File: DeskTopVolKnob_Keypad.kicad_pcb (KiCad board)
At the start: 2 copper layers, 118.4 x 101.6 mm, 105 parts, among them J1 DX07S016JA1R1500, SW1 Rotary_Encoder_Switch, SW10 SW, SW11 SW, SW12 SW, SW13 SW, SW14 SW, SW15 SW, SW16 SW, SW17 SW, SW18 SW, SW19 SW, SW2 SW, SW20 SW, SW21 SW, SW22 SW, SW23 SW, SW24 SW, SW25 SW, SW26 SW, SW27 SW_Push, SW3 SW, SW4 SW, SW5 SW, SW6 SW, SW7 SW, SW8 SW, SW9 SW, U1 ATmega32U4-AU, Y1 16MHz

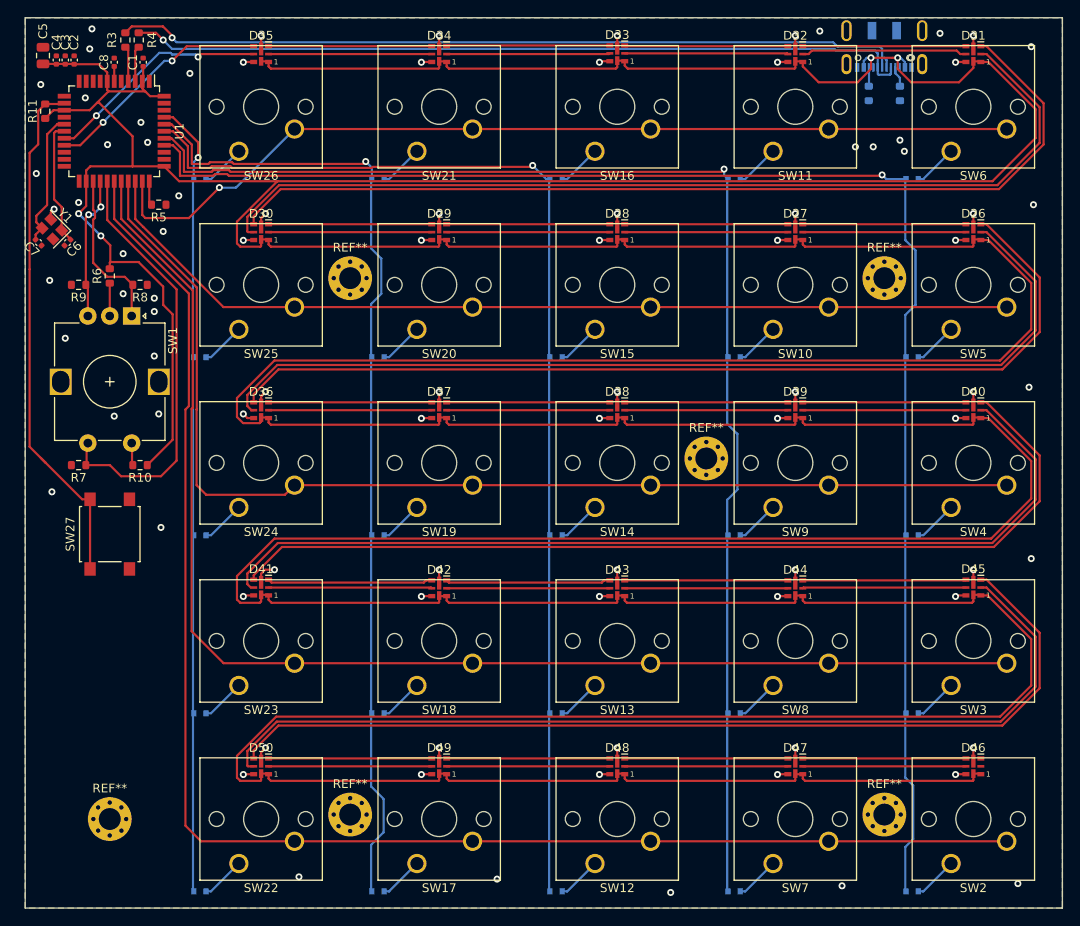
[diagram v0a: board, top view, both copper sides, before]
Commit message: new LEDs and crystal cap fixed
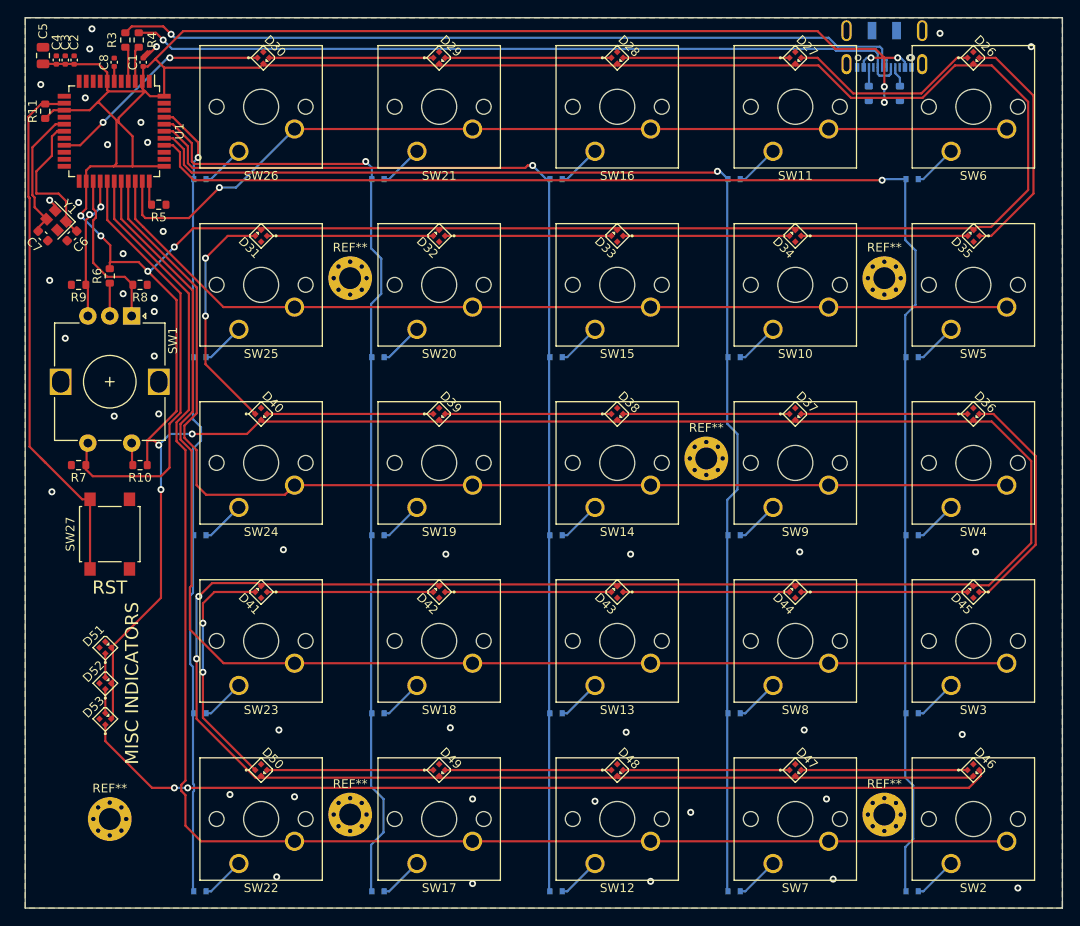
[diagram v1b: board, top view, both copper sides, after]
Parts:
- added D51: SK6805-EC-15, Special Partd:SK6805-EC-15, F.Cu at (45.7, 99.8)
- added D52: SK6805-EC-15, Special Partd:SK6805-EC-15, F.Cu at (45.7, 103.9)
- added D53: SK6805-EC-15, Special Partd:SK6805-EC-15, F.Cu at (45.7, 108.0)
- C6, C7: footprint Capacitor_SMD:C_0402_1005Metric -> Capacitor_SMD:C_0603_1608Metric
- D26, D27, D28, D29, D30, D31, D32, D33, D34, D35, D36, D37, D38, D39, D40, D41, D42, D43, D44, D45, D46, D47, D48, D49, D50: value APA102-2020 -> SK6805-EC-15; footprint LED_SMD:LED-APA102-2020 -> Special Partd:SK6805-EC-15
- SW10, SW11, SW12, SW13, SW14, SW15, SW16, SW17, SW18, SW19, SW2, SW20, SW21, SW22, SW23, SW24, SW25, SW26, SW3, SW4, SW5, SW6, SW7, SW8, SW9: footprint Downloaded parts:SW_Cherry_MX_1.00u_PCB -> Button_Switch_Keyboard:SW_Cherry_MX_1.00u_PCB
- moved D35 83.9 mm to (144.8, 52.8), turned to 135 degrees
- moved D31 83.9 mm to (63.5, 52.8), turned to 135 degrees
- moved D36 81.3 mm to (144.8, 73.2), turned to 315 degrees
- moved D40 81.3 mm to (63.5, 73.2), turned to 315 degrees
- moved D32 45.6 mm to (83.8, 52.8), turned to 135 degrees
- moved D34 45.6 mm to (124.5, 52.8), turned to 135 degrees
- moved D37 40.6 mm to (124.5, 73.2), turned to 315 degrees
- moved D39 40.6 mm to (83.8, 73.2), turned to 315 degrees
- moved D33 20.8 mm to (104.1, 52.8), turned to 135 degrees
- moved D30 19.9 mm to (63.8, 32.5), turned to 315 degrees
- moved D26 19.9 mm to (144.8, 32.5), turned to 315 degrees
- moved D27 19.9 mm to (124.5, 32.5), turned to 315 degrees
- moved D28 19.9 mm to (104.1, 32.5), turned to 315 degrees
- moved D29 19.9 mm to (83.8, 32.5), turned to 315 degrees
- moved Y1 1.14 mm to (40.1, 51.1)
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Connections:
- D26 pad 1: +5V -> Net-(D26-Pad1)
- D26 pad 2: Net-(D26-Pad2) -> +5V
- D26 pad 4: Net-(D26-Pad4) -> GND
- D27 pad 1: +5V -> Net-(D27-Pad1)
- D27 pad 2: Net-(D26-Pad5) -> +5V
- D27 pad 3: Net-(D26-Pad4) -> Net-(D26-Pad1)
- D27 pad 4: Net-(D27-Pad4) -> GND
- D28 pad 1: +5V -> Net-(D28-Pad1)
- D28 pad 2: Net-(D27-Pad5) -> +5V
- D28 pad 3: Net-(D27-Pad4) -> Net-(D27-Pad1)
- D28 pad 4: Net-(D28-Pad4) -> GND
- D29 pad 1: +5V -> Net-(D29-Pad1)
- D29 pad 2: Net-(D28-Pad5) -> +5V
- D29 pad 3: Net-(D28-Pad4) -> Net-(D28-Pad1)
- D29 pad 4: Net-(D29-Pad4) -> GND
- D30 pad 1: +5V -> /LEDs/SD
- D30 pad 2: Net-(D29-Pad5) -> +5V
- D30 pad 3: Net-(D29-Pad4) -> Net-(D29-Pad1)
- D30 pad 4: Net-(D30-Pad4) -> GND
- D31 pad 1: +5V -> Net-(D31-Pad1)
- D31 pad 2: Net-(D30-Pad5) -> +5V
- D31 pad 3: Net-(D30-Pad4) -> Net-(D31-Pad3)
- D31 pad 4: Net-(D31-Pad4) -> GND
- D32 pad 1: +5V -> Net-(D32-Pad1)
- D32 pad 2: Net-(D31-Pad5) -> +5V
- D32 pad 3: Net-(D31-Pad4) -> Net-(D31-Pad1)
- D32 pad 4: Net-(D32-Pad4) -> GND
- D33 pad 1: +5V -> Net-(D33-Pad1)
- D33 pad 2: Net-(D32-Pad5) -> +5V
- D33 pad 3: Net-(D32-Pad4) -> Net-(D32-Pad1)
- D33 pad 4: Net-(D33-Pad4) -> GND
- D34 pad 1: +5V -> Net-(D34-Pad1)
- D34 pad 2: Net-(D33-Pad5) -> +5V
- D34 pad 3: Net-(D33-Pad4) -> Net-(D33-Pad1)
- D34 pad 4: Net-(D34-Pad4) -> GND
- D35 pad 1: +5V -> Net-(D26-Pad3)
- D35 pad 2: Net-(D34-Pad5) -> +5V
- D35 pad 3: Net-(D34-Pad4) -> Net-(D34-Pad1)
- D35 pad 4: /LEDs/SD -> GND
- D36 pad 1: +5V -> Net-(D36-Pad1)
- D36 pad 2: Net-(D36-Pad2) -> +5V
- D36 pad 4: Net-(D26-Pad3) -> GND
- D37 pad 1: +5V -> Net-(D37-Pad1)
- D37 pad 2: Net-(D37-Pad2) -> +5V
- D37 pad 3: Net-(D37-Pad3) -> Net-(D36-Pad1)
- D37 pad 4: Net-(D36-Pad3) -> GND
- D38 pad 1: +5V -> Net-(D38-Pad1)
- D38 pad 2: Net-(D38-Pad2) -> +5V
- D38 pad 3: Net-(D38-Pad3) -> Net-(D37-Pad1)
- D38 pad 4: Net-(D37-Pad3) -> GND
- D39 pad 1: +5V -> Net-(D39-Pad1)
- D39 pad 2: Net-(D39-Pad2) -> +5V
- D39 pad 3: Net-(D39-Pad3) -> Net-(D38-Pad1)
- D39 pad 4: Net-(D38-Pad3) -> GND
- D40 pad 1: +5V -> Net-(D31-Pad3)
- D40 pad 2: Net-(D40-Pad2) -> +5V
- D40 pad 3: Net-(D40-Pad3) -> Net-(D39-Pad1)
- D40 pad 4: Net-(D39-Pad3) -> GND
- D41 pad 1: +5V -> Net-(D41-Pad1)
- D41 pad 2: Net-(D41-Pad2) -> +5V
- D41 pad 4: Net-(D40-Pad3) -> GND
- D42 pad 1: +5V -> Net-(D42-Pad1)
- D42 pad 2: Net-(D42-Pad2) -> +5V
- D42 pad 3: Net-(D42-Pad3) -> Net-(D41-Pad1)
- D42 pad 4: Net-(D41-Pad3) -> GND
- D43 pad 1: +5V -> Net-(D43-Pad1)
- D43 pad 2: Net-(D43-Pad2) -> +5V
- D43 pad 3: Net-(D43-Pad3) -> Net-(D42-Pad1)
- D43 pad 4: Net-(D42-Pad3) -> GND
- D44 pad 1: +5V -> Net-(D44-Pad1)
- D44 pad 2: Net-(D44-Pad2) -> +5V
- D44 pad 3: Net-(D44-Pad3) -> Net-(D43-Pad1)
- D44 pad 4: Net-(D43-Pad3) -> GND
- D45 pad 1: +5V -> Net-(D36-Pad3)
- D45 pad 2: Net-(D45-Pad2) -> +5V
- D45 pad 3: Net-(D45-Pad3) -> Net-(D44-Pad1)
- D45 pad 4: Net-(D44-Pad3) -> GND
- D46 pad 1: +5V -> Net-(D46-Pad1)
- D46 pad 2: (no net) -> +5V
- D46 pad 3: (no net) -> Net-(D46-Pad3)
- D46 pad 4: Net-(D46-Pad4) -> GND
- D47 pad 1: +5V -> Net-(D47-Pad1)
- D47 pad 2: Net-(D46-Pad5) -> +5V
- D47 pad 3: Net-(D46-Pad4) -> Net-(D46-Pad1)
- D47 pad 4: Net-(D47-Pad4) -> GND
- D48 pad 1: +5V -> Net-(D48-Pad1)
- D48 pad 2: Net-(D47-Pad5) -> +5V
- D48 pad 3: Net-(D47-Pad4) -> Net-(D47-Pad1)
- D48 pad 4: Net-(D48-Pad4) -> GND
- D49 pad 1: +5V -> Net-(D49-Pad1)
- D49 pad 2: Net-(D48-Pad5) -> +5V
- D49 pad 3: Net-(D48-Pad4) -> Net-(D48-Pad1)
- D49 pad 4: Net-(D49-Pad4) -> GND
- D50 pad 1: +5V -> Net-(D41-Pad3)
- D50 pad 2: Net-(D49-Pad5) -> +5V
- D50 pad 3: Net-(D49-Pad4) -> Net-(D49-Pad1)
- D50 pad 4: Net-(D45-Pad3) -> GND
- J1 pad 10: (no net) -> Net-(J1-Pad10)
- J1 pad 4: (no net) -> Net-(J1-Pad4)
- U1 pad 1: (no net) -> Net-(U1-Pad1)
- U1 pad 10: (no net) -> Net-(U1-Pad10)
- U1 pad 11: (no net) -> Net-(U1-Pad11)
- U1 pad 12: (no net) -> Net-(U1-Pad12)
- U1 pad 18: /LEDs/CK -> Net-(U1-Pad18)
- U1 pad 20: (no net) -> Net-(U1-Pad20)
- U1 pad 21: (no net) -> Net-(U1-Pad21)
- U1 pad 22: (no net) -> Net-(U1-Pad22)
- U1 pad 36: (no net) -> Net-(U1-Pad36)
- U1 pad 42: (no net) -> Net-(U1-Pad42)
- U1 pad 8: (no net) -> Net-(U1-Pad8)
- U1 pad 9: (no net) -> Net-(U1-Pad9)
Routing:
- net +5V: track 1001.5 -> 775.1 mm, vias 4 -> 13
- net Net-(D45-Pad2): track 109.7 -> 0.00 mm
- net Net-(D30-Pad5): track 109.6 -> 0.00 mm
- net Net-(D26-Pad2): track 109.4 -> 0.00 mm
- net Net-(D45-Pad3): track 109.1 -> 0.00 mm
- net Net-(D30-Pad4): track 109.0 -> 0.00 mm
- net Net-(D40-Pad2): track 108.4 -> 0.00 mm
- net Net-(D40-Pad3): track 108.1 -> 0.00 mm
- net Net-(D46-Pad3): track 0.00 -> 105.3 mm, vias 0 -> 2
- net Net-(D26-Pad3): track 109.0 -> 27.3 mm
- net GND: track 71.3 -> 5.60 mm, vias 89 -> 44
- net Net-(D31-Pad3): track 0.00 -> 26.9 mm, vias 0 -> 2
- net /LEDs/CK: track 26.0 -> 0.00 mm, vias 2 -> 0
- net Net-(D26-Pad1): track 0.00 -> 22.3 mm
- net Net-(D34-Pad1): track 0.00 -> 19.0 mm
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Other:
- board text added: "2.5mm"
- board text added: "MISC INDICATORS"
- board text added: "RST"
